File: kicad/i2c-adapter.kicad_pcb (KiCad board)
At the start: 2 copper layers, 98.4 x 65 mm, 49 parts, among them J1 Conn_02x13_Top_Bottom, J10 AUX IN, J11 +5V, J2 I2C-1, J3 I2C-2, J4 I2C-3, J5 I2C-4, J6 SPI-1, J7 SPI-2, J8 SPI-3, J9 SPI-4, U1 74HC05, U2 74HC244, U3 LM1117-3.3

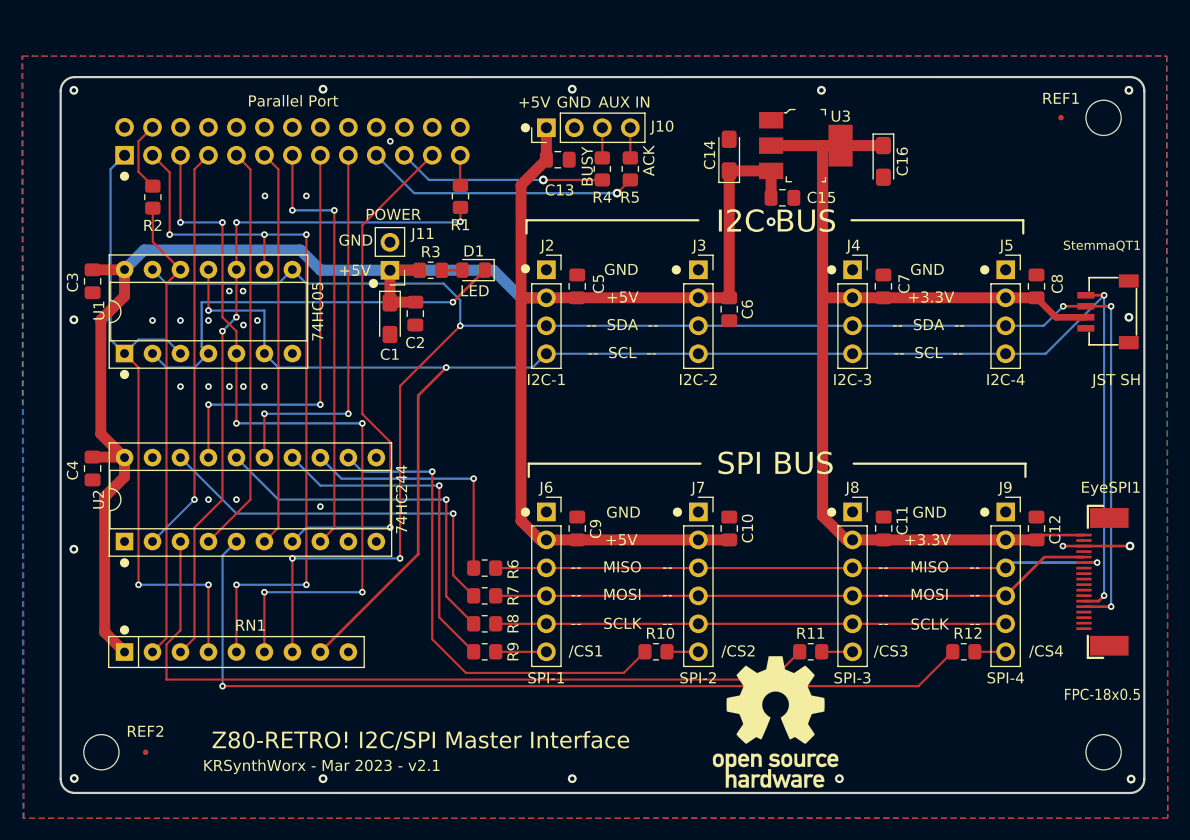
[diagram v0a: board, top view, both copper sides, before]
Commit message: With the help of @K3130440, I've added level shifters to the 3V3 data lines and a 74HC138 which adds more Chip Select lines (that are then routed to the EyeSPI connector). Updated Schematic PDF to include the hardware changes. I moved the major ICs closer together to save on board space. Current Board size: 98 x 66.3; Via count: 52; I tried to make sure many components have a position as close to a whole number as possible. Added 3D models to shorten the height of the I2C/SPI proto area. Updated the chips to have a stacked 3D Models structure and added text to each chip. Updated 3D render with the updated 3D Models. Quite a few of the .asm files in src/ need to be updated with the hardware changes.
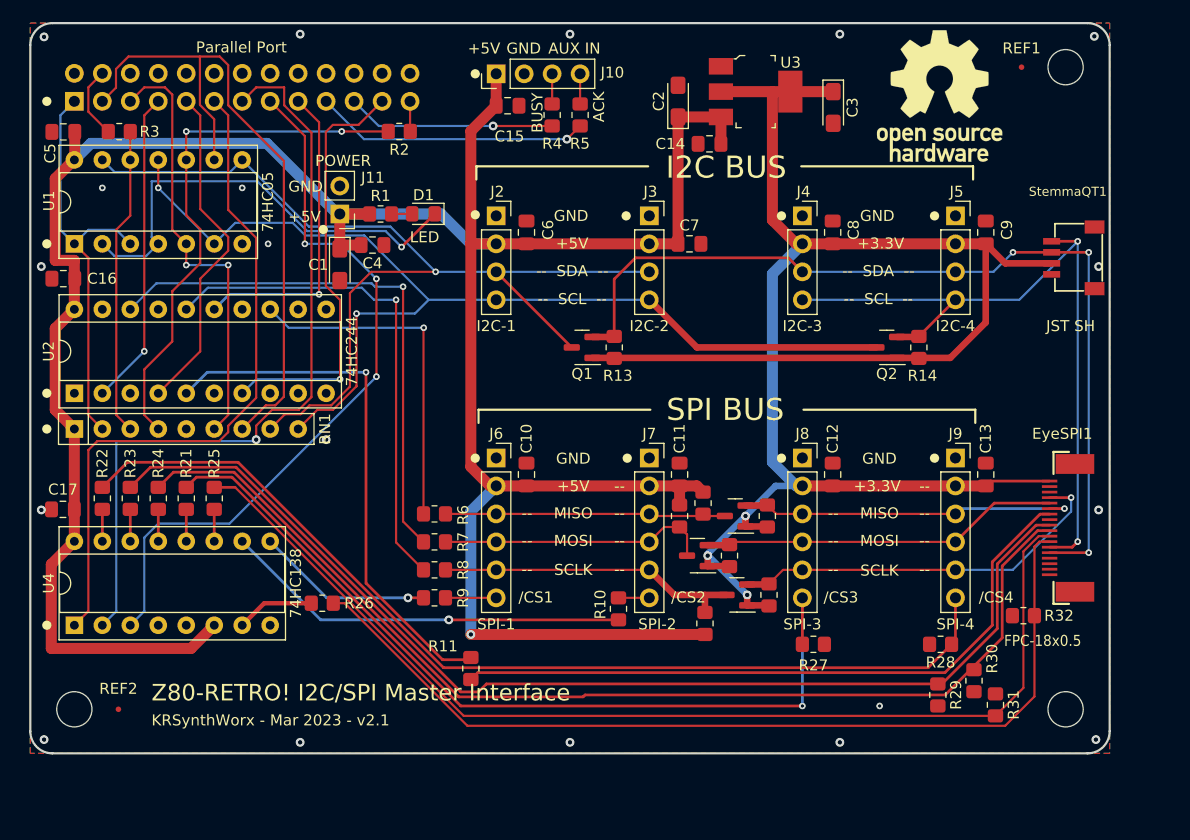
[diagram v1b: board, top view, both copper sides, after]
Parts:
- removed R12: 330, Resistor_SMD:R_0805_2012Metric_Pad1.20x1.40mm_HandSolder
- added C17: 0.1uF, Capacitor_SMD:C_0805_2012Metric_Pad1.18x1.45mm_HandSolder, F.Cu at (93.0, 104.1)
- added Q1: BSS138, Package_TO_SOT_SMD:SOT-23, F.Cu at (140.1, 89.4)
- added Q2: BSS138, Package_TO_SOT_SMD:SOT-23, F.Cu at (167.8, 89.4)
- added Q3: BSS138, Package_TO_SOT_SMD:SOT-23, F.Cu at (154.0, 104.8)
- added Q4: BSS138, Package_TO_SOT_SMD:SOT-23, F.Cu at (150.6, 108.3)
- added Q5: BSS138, Package_TO_SOT_SMD:SOT-23, F.Cu at (154.2, 111.9)
- added R13: 10K, Resistor_SMD:R_0805_2012Metric_Pad1.20x1.40mm_HandSolder, F.Cu at (143.0, 89.4)
- added R14: 10K, Resistor_SMD:R_0805_2012Metric_Pad1.20x1.40mm_HandSolder, F.Cu at (170.7, 89.4)
- added R15: 10K, Resistor_SMD:R_0805_2012Metric_Pad1.20x1.40mm_HandSolder, F.Cu at (151.1, 103.6)
- added R16: 10K, Resistor_SMD:R_0805_2012Metric_Pad1.20x1.40mm_HandSolder, F.Cu at (156.9, 104.8)
- added R17: 10K, Resistor_SMD:R_0805_2012Metric_Pad1.20x1.40mm_HandSolder, F.Cu at (148.9, 104.8)
- added R18: 10K, Resistor_SMD:R_0805_2012Metric_Pad1.20x1.40mm_HandSolder, F.Cu at (153.5, 108.3)
- added R19: 10K, Resistor_SMD:R_0805_2012Metric_Pad1.20x1.40mm_HandSolder, F.Cu at (151.3, 114.5)
- added R20: 10K, Resistor_SMD:R_0805_2012Metric_Pad1.20x1.40mm_HandSolder, F.Cu at (157.1, 111.9)
- added R21: 2K7, Resistor_SMD:R_0805_2012Metric_Pad1.20x1.40mm_HandSolder, F.Cu at (104.2, 103.1)
- added R22: 2K7, Resistor_SMD:R_0805_2012Metric_Pad1.20x1.40mm_HandSolder, F.Cu at (96.5, 103.1)
- added R23: 2K7, Resistor_SMD:R_0805_2012Metric_Pad1.20x1.40mm_HandSolder, F.Cu at (99.1, 103.1)
- added R24: 2K7, Resistor_SMD:R_0805_2012Metric_Pad1.20x1.40mm_HandSolder, F.Cu at (101.6, 103.1)
- added R25: 2K7, Resistor_SMD:R_0805_2012Metric_Pad1.20x1.40mm_HandSolder, F.Cu at (106.7, 103.1)
- added R26: 2K7, Resistor_SMD:R_0805_2012Metric_Pad1.20x1.40mm_HandSolder, F.Cu at (116.5, 112.7)
- added R27: 4K7, Resistor_SMD:R_0805_2012Metric_Pad1.20x1.40mm_HandSolder, F.Cu at (161.1, 116.4)
- added R28: 4K7, Resistor_SMD:R_0805_2012Metric_Pad1.20x1.40mm_HandSolder, F.Cu at (172.6, 116.4)
- added R29: 4K7, Resistor_SMD:R_0805_2012Metric_Pad1.20x1.40mm_HandSolder, F.Cu at (172.4, 121.0)
- added R30: 4K7, Resistor_SMD:R_0805_2012Metric_Pad1.20x1.40mm_HandSolder, F.Cu at (175.7, 119.7)
- added R31: 4K7, Resistor_SMD:R_0805_2012Metric_Pad1.20x1.40mm_HandSolder, F.Cu at (177.6, 121.9)
- added R32: 4K7, Resistor_SMD:R_0805_2012Metric_Pad1.20x1.40mm_HandSolder, F.Cu at (180.2, 113.8)
- added REF**: OSHW-Logo_11.4x12mm_SilkScreen, Symbol:OSHW-Logo_11.4x12mm_SilkScreen, F.Cu at (172.6, 66.6)
- added U4: 74HC138, Package_DIP:DIP-16_W7.62mm_Socket, F.Cu at (94.0, 114.7)
- REF**: moved to B.Cu
- moved R11 30.9 mm to (130.0, 118.6), turned to -90 degrees
- moved RN1 20.8 mm to (94.0, 96.8)
- moved C16 17.4 mm to (93.0, 83.2), turned to 180 degrees
- moved U2 14.2 mm to (94.0, 93.6)
- moved C5 13.8 mm to (93.0, 69.9), turned to 180 degrees
- moved U1 11.0 mm to (94.0, 80.0)
- moved C14 8.24 mm to (151.7, 71.0), turned to 180 degrees
- moved R2 8.10 mm to (123.5, 69.8), turned to 180 degrees
- moved C4 7.34 mm to (121.1, 80.2), turned to 0 degrees
- moved C7 6.95 mm to (149.8, 80.0), turned to 0 degrees
- moved D1 6.85 mm to (125.7, 77.3)
- moved J11 6.85 mm to (118.1, 77.3)
- moved R1 6.85 mm to (121.8, 77.3)
- moved C2 6.75 mm to (148.8, 67.1)
- moved C12 6.74 mm to (162.8, 101.0)
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- renumbered C9 to C10, C10 to C11, C11 to C12, C12 to C13, C15 to C14, C13 to C15, C4 to C16, C14 to C2, C16 to C3, C2 to C4, C3 to C5, C5 to C6, C6 to C7, C7 to C8, C8 to C9, R3 to R1, R1 to R2, R2 to R3
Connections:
- net Net-(J1-Pad13) renamed /STATUS
- net Net-(J1-Pad15) renamed /ERROR
- net Net-(J1-Pad3) renamed /D1
- EyeSPI1 pad 10: unconnected-(EyeSPI1-Pad10) -> /CARDCS
- EyeSPI1 pad 11: unconnected-(EyeSPI1-Pad11) -> /MEM_CS
- EyeSPI1 pad 12: unconnected-(EyeSPI1-Pad12) -> /TSCS
- EyeSPI1 pad 13: /SCL -> /SCL3V
- EyeSPI1 pad 14: /SDA -> /SDA3V
- EyeSPI1 pad 4: /SCK -> /SCLK3V
- EyeSPI1 pad 5: /MOSI -> /MOSI3V
- EyeSPI1 pad 6: /MISO -> /MISO3V
- EyeSPI1 pad 7: unconnected-(EyeSPI1-Pad7) -> /TFTDC
- EyeSPI1 pad 9: unconnected-(EyeSPI1-Pad9) -> /TFTCS
- J1 pad 1: Net-(J1-Pad1) -> /RNP2
- J1 pad 2: Net-(J1-Pad2) -> /D0
- J2 pad 3: /SDA -> /RNP8
- J2 pad 4: /SCL -> /RNP9
- J3 pad 3: /SDA -> /RNP8
- J3 pad 4: /SCL -> /RNP9
- J4 pad 3: /SDA -> /SDA3V
- J4 pad 4: /SCL -> /SCL3V
- J5 pad 3: /SDA -> /SDA3V
- J5 pad 4: /SCL -> /SCL3V
- J8 pad 3: /MISO -> /MISO3V
- J8 pad 4: /MOSI -> /MOSI3V
- J8 pad 5: /SCLK -> /SCLK3V
- J8 pad 6: /~{CS3} -> /~{CS3}-3V
- J9 pad 3: /MISO -> /MISO3V
- J9 pad 4: /MOSI -> /MOSI3V
- J9 pad 5: /SCLK -> /SCLK3V
- J9 pad 6: /~{CS4} -> /~{CS4}-3V
- R11 pad 2: /~{CS3} -> /TFTDC
- R2 pad 2: Net-(R1-Pad2) -> /RNP4
- R3 pad 2: Net-(R2-Pad2) -> /RNP3
- RN1 pad 2: Net-(R2-Pad2) -> /RNP2
- RN1 pad 3: Net-(R1-Pad2) -> /RNP3
- RN1 pad 4: Net-(J1-Pad1) -> /RNP4
- RN1 pad 5: Net-(J1-Pad2) -> /RNP5
- RN1 pad 7: /SDA -> /D0
- RN1 pad 8: /SCL -> /RNP8
- RN1 pad 9: unconnected-(RN1-Pad9) -> /RNP9
- StemmaQT1 pad 3: /SDA -> /SDA3V
- StemmaQT1 pad 4: /SCL -> /SCL3V
- U1 pad 1: Net-(J1-Pad1) -> /RNP2
- U1 pad 10: Net-(R1-Pad2) -> /RNP4
- U1 pad 11: /SCL -> /RNP9
- U1 pad 12: Net-(R2-Pad2) -> /RNP3
- U1 pad 13: /SDA -> /RNP8
- U1 pad 3: Net-(J1-Pad1) -> /RNP2
- U1 pad 6: /SCL -> /RNP9
- U1 pad 8: /SDA -> /RNP8
- U1 pad 9: Net-(J1-Pad2) -> /D0
- U2 pad 12: Net-(R10-Pad1) -> unconnected-(U2-Pad12)
- U2 pad 14: Net-(R9-Pad1) -> unconnected-(U2-Pad14)
- U2 pad 17: /D6 -> GND
- U2 pad 3: Net-(R11-Pad1) -> unconnected-(U2-Pad3)
- U2 pad 5: Net-(R12-Pad1) -> Net-(R11-Pad1)
- U2 pad 6: /D4 -> GND
- U2 pad 8: /D5 -> GND
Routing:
- net /SDA: track 163.7 -> 0.00 mm, vias 6 -> 0
- net /SCL: track 153.7 -> 0.00 mm, vias 4 -> 0
- net /TFTCS: track 0.00 -> 102.4 mm
- net /CARDCS: track 0.00 -> 100.0 mm
- net /MEM_CS: track 0.00 -> 98.5 mm
- net /RNP9: track 0.00 -> 95.8 mm, vias 0 -> 2
- net /~{CS4}-3V: track 0.00 -> 91.0 mm
- net /RNP8: track 0.00 -> 90.4 mm, vias 0 -> 1
- net /TSCS: track 0.00 -> 84.5 mm
- net /SDA3V: track 0.00 -> 83.1 mm, vias 0 -> 3
- net Net-(R12-Pad1): track 81.2 -> 0.00 mm, vias 1 -> 0
- net /~{CS3}-3V: track 0.00 -> 79.0 mm, vias 0 -> 1
- net +3V3: track 93.3 -> 165.4 mm, vias 0 -> 3
- net Net-(J1-Pad2): track 67.6 -> 0.00 mm, vias 5 -> 0
- net /SCL3V: track 0.00 -> 66.3 mm, vias 0 -> 2
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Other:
- board size 98.4 x 65 mm -> 98 x 66.3 mm

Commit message: Updated BOM.  Most parts are available from both LCSC and DigiKey. Added Teardrops to PCB.
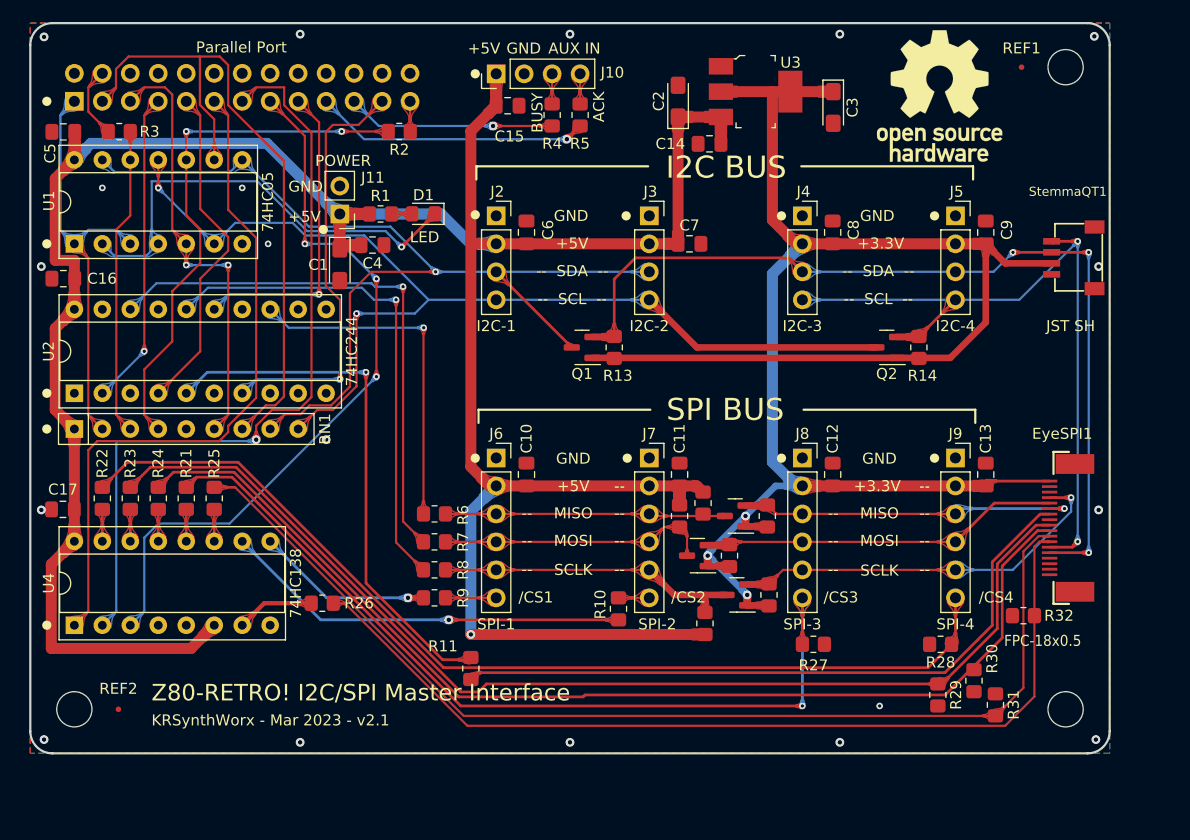
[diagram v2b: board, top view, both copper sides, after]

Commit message: Enhanced 3D Models and render; Moved away from Tantalum footprint.
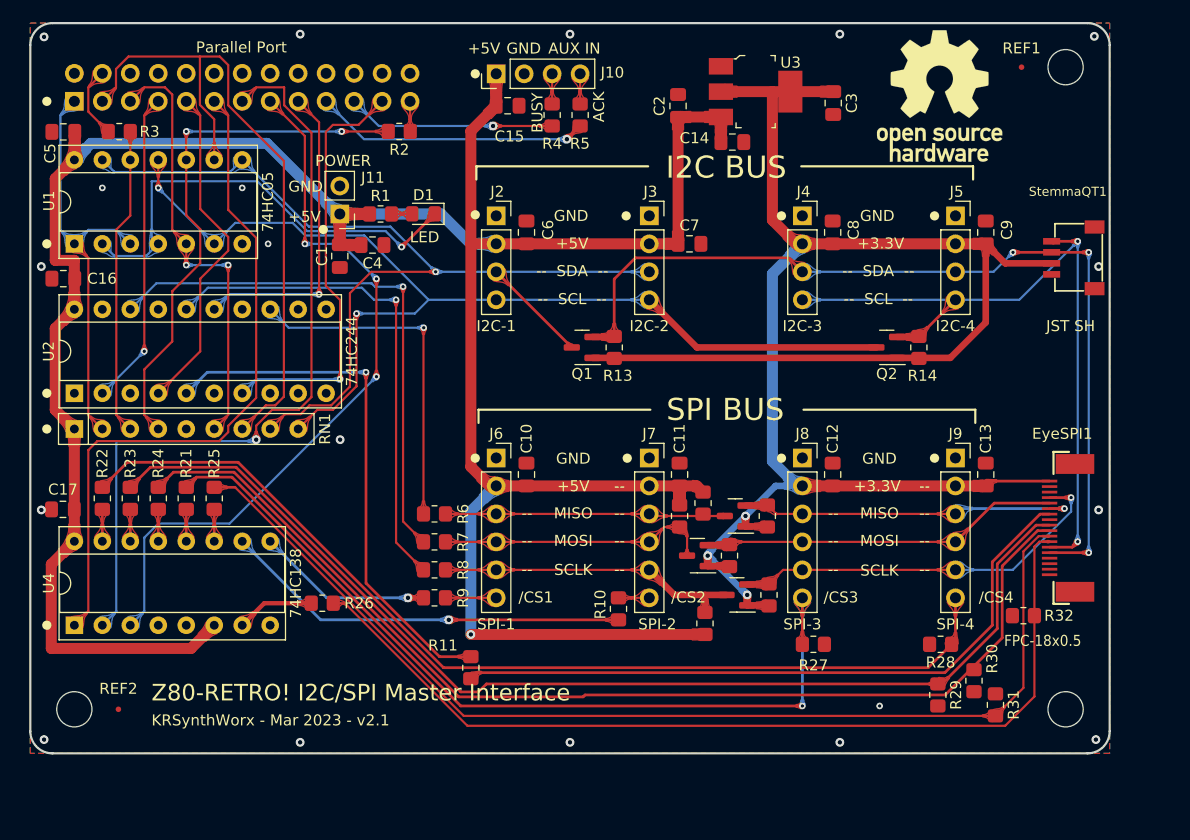
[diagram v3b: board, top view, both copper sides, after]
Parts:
- C1, C2, C3: footprint Capacitor_Tantalum_SMD:CP_EIA-3216-10_Kemet-I_Pad1.58x1.35mm_HandSolder -> Capacitor_SMD:C_0805_2012Metric_Pad1.18x1.45mm_HandSolder
- moved C14 2.08 mm to (153.7, 70.8), turned to 0 degrees
- moved C1 0.79 mm to (118.1, 81.2)
- moved C2 0.44 mm to (148.8, 67.5)
- moved C3 0.40 mm to (162.9, 67.3)
- moved R11 0.08 mm to (130.0, 118.5), turned to 90 degrees
- turned R15 to 90 degrees
- turned R17 to 90 degrees
- turned R2 to 0 degrees
- turned R28 to 0 degrees
- turned R29 to 90 degrees
- turned R30 to 90 degrees
- turned R32 to 0 degrees
- turned R6 to 0 degrees
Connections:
- R11 pad 1: Net-(R11-Pad1) -> /TFTDC
- R11 pad 2: /TFTDC -> Net-(R11-Pad2)
- R15 pad 1: +5V -> /MISO
- R15 pad 2: /MISO -> +5V
- R17 pad 1: +5V -> /MOSI
- R17 pad 2: /MOSI -> +5V
- R2 pad 1: /STATUS -> /RNP4
- R2 pad 2: /RNP4 -> /STATUS
- R28 pad 1: /~{CS4}-3V -> GND
- R28 pad 2: GND -> /~{CS4}-3V
- R29 pad 1: /TFTCS -> GND
- R29 pad 2: GND -> /TFTCS
- R30 pad 1: /CARDCS -> GND
- R30 pad 2: GND -> /CARDCS
- R32 pad 1: /TSCS -> GND
- R32 pad 2: GND -> /TSCS
- R6 pad 1: /MISO -> Net-(R6-Pad1)
- R6 pad 2: Net-(R6-Pad2) -> /MISO
- U2 pad 13: Net-(R6-Pad2) -> Net-(R6-Pad1)
- U2 pad 5: Net-(R11-Pad1) -> Net-(R11-Pad2)
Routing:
- net Net-(R11-Pad1): track 48.7 -> 0.00 mm, vias 1 -> 0
- net Net-(R11-Pad2): track 0.00 -> 48.5 mm, vias 0 -> 1
- net Net-(R6-Pad2): track 31.5 -> 0.00 mm, vias 1 -> 0
- net Net-(R6-Pad1): track 0.00 -> 31.5 mm, vias 0 -> 1
- net +5V: track 250.6 -> 250.0 mm
